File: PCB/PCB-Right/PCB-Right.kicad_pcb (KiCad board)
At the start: 2 copper layers, 109.8 x 71.7 mm, 53 parts, among them J1 USB_C_Receptacle_USB2.0_16P, J2 Conn_ARM_JTAG_SWD_10, Q1 2N7002, SW1 SW_RST, SW2 SW_SPDT, U1 nRF52840_holyiot_18010, U2 XC6206PxxxMR, U3 SRV05-4, U4 BQ24075RGT

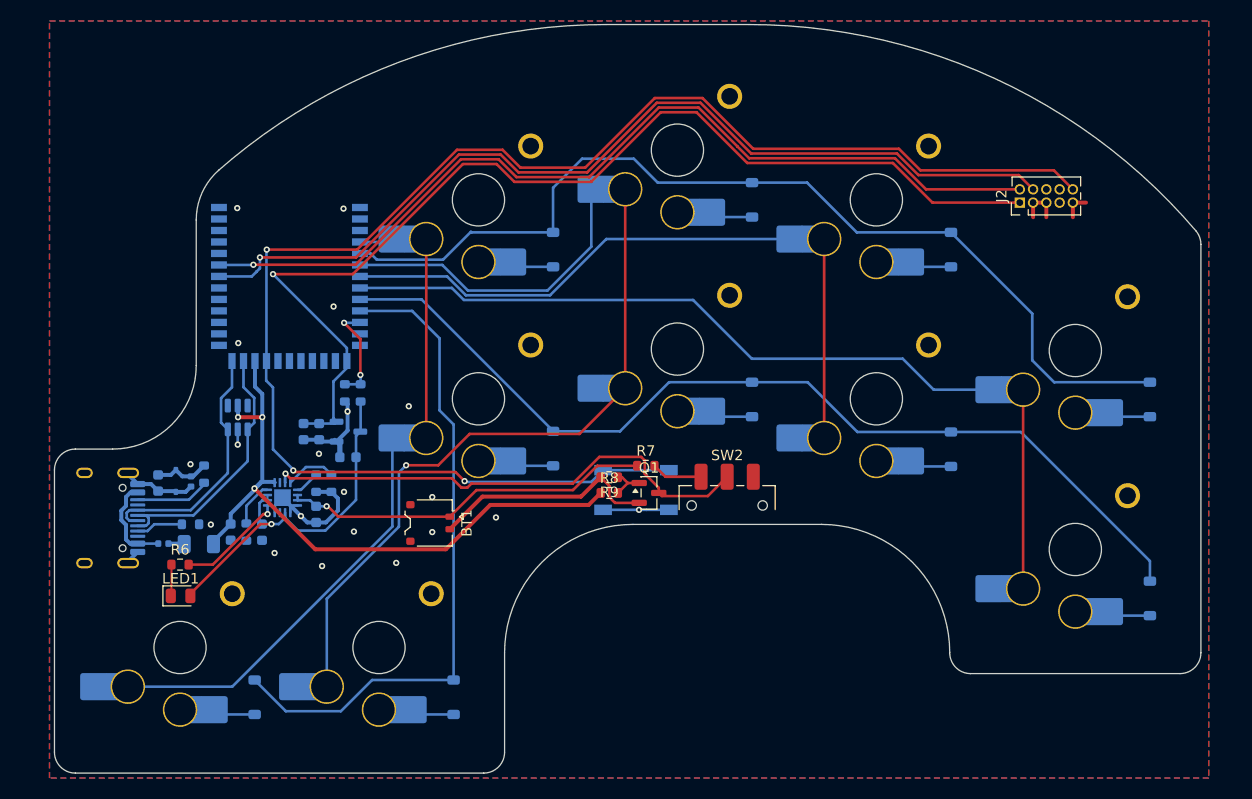
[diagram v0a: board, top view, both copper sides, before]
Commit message: PCB Right
Switched to raytac module
gasket mount
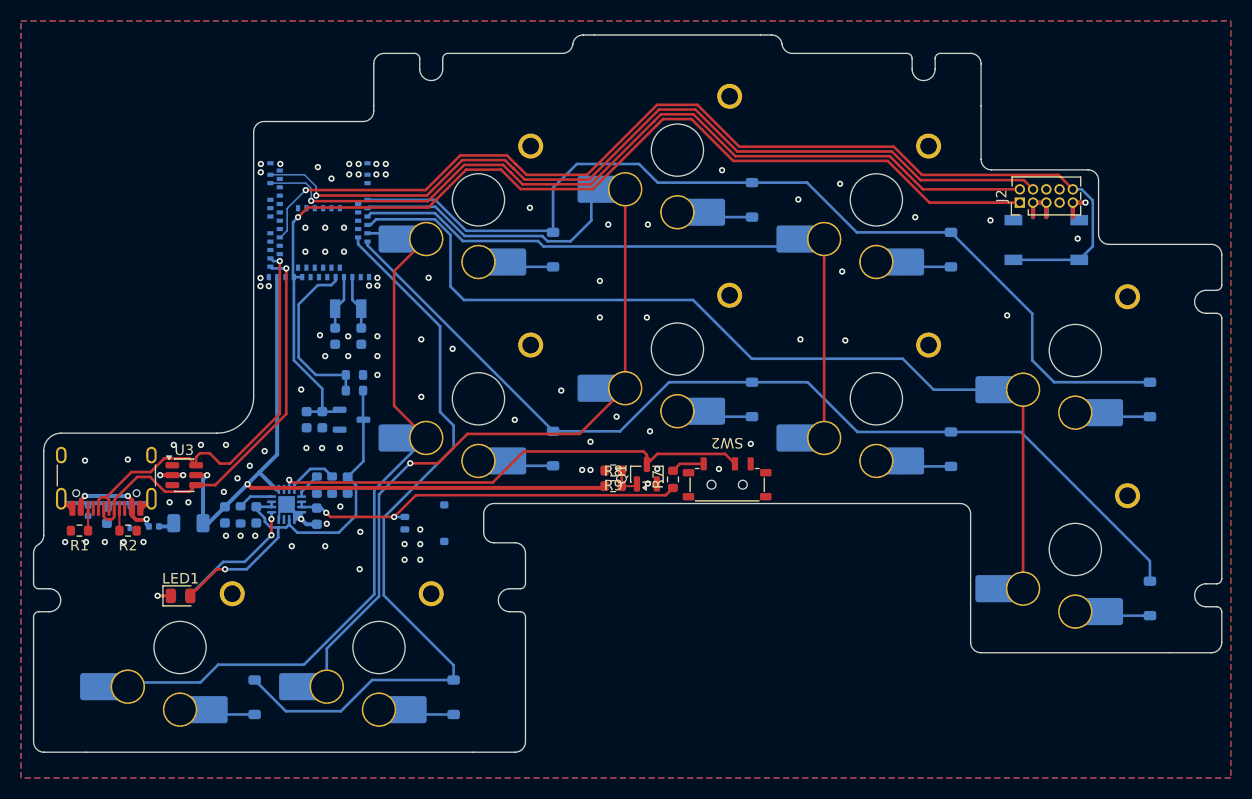
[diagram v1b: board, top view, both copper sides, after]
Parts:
- removed U1: nRF52840_holyiot_18010, marbastlib-various:nRF52840_holyiot_18010_HS_simple
- added C8: 12p, Capacitor_SMD:C_0603_1608Metric, B.Cu at (144.3, 97.2)
- added C9: 12p, Capacitor_SMD:C_0603_1608Metric, B.Cu at (141.8, 97.2)
- added U5: MDBT50Q-1MV2, RF_Module:Raytac_MDBT50Q, B.Cu at (140.3, 84.4)
- added Y1: 32.768KHz, Crystal:Crystal_SMD_3215-2Pin_3.2x1.5mm, B.Cu at (143.1, 94.6)
- BT1, R6: moved to B.Cu
- J1: footprint Connector_USB:USB_C_Receptacle_HRO_TYPE-C-31-M-12 -> marbastlib-various:USB_C_Receptacle_HRO_TYPE-C-31-M-12; moved to F.Cu
- R1, R2, U3: moved to F.Cu
- SW2: footprint Button_Switch_SMD:SW_SPDT_CK_JS102011SAQN -> marbastlib-various:SW_MSK12C02-HB
- moved SW1 46.0 mm to (209.9, 88.0), turned to 0 degrees
- moved R1 13.1 mm to (117.4, 115.8), turned to 180 degrees
- moved L2 10.2 mm to (118.2, 113.9), turned to -90 degrees
- moved U3 7.54 mm to (127.4, 110.5), turned to 0 degrees
- moved R2 6.01 mm to (122.0, 115.8)
- moved C4 5.79 mm to (120.0, 114.3), turned to 90 degrees
- moved D11 5.60 mm to (122.2, 114.5), turned to -90 degrees
- moved J1 5.08 mm to (119.9, 109.6), turned to 180 degrees
- moved R6 2.99 mm to (127.0, 122.1)
- moved R7 2.91 mm to (174.2, 110.9), turned to 90 degrees
- moved C1 2.67 mm to (143.1, 111.5), turned to -90 degrees
- moved F1 2.24 mm to (127.8, 115.1)
- moved SW2 1.99 mm to (179.4, 111.4), turned to 180 degrees
- moved R11 1.95 mm to (143.7, 100.9), turned to 0 degrees
- moved L1 1.87 mm to (124.5, 115.4)
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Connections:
- U3 pad 1: USB-D- -> unconnected-(U3-IO1-Pad1)
- U3 pad 3: USB-D+ -> unconnected-(U3-IO2-Pad3)
- U3 pad 4: unconnected-(U3-IO3-Pad4) -> USB-D-
- U3 pad 6: unconnected-(U3-IO4-Pad6) -> USB-D+
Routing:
- net RST: track 147.4 -> 102.2 mm, vias 3 -> 1
- net GND: track 66.0 -> 27.8 mm, vias 20 -> 101
- net USB-D+: track 24.3 -> 40.2 mm, vias 0 -> 1
- net USB-D-: track 25.8 -> 40.2 mm, vias 0 -> 1
- net row2: track 63.5 -> 73.2 mm
- net SWDCLK: track 90.3 -> 82.5 mm
- net VSENSE: track 9.58 -> 16.4 mm, vias 2 -> 0
- net SWDIO: track 87.6 -> 81.1 mm
- net +5V: track 63.3 -> 69.7 mm, vias 3 -> 2
- net col0: track 62.4 -> 68.2 mm
- net XL2: track 0.00 -> 5.23 mm
- net XL1: track 0.00 -> 5.23 mm
- net col3: track 83.3 -> 88.5 mm
- net Net-(J1-CC2): track 7.13 -> 2.14 mm
- net +VSW: track 35.5 -> 39.6 mm
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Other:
- board size 109.8 x 71.7 mm -> 113.8 x 68.7 mm

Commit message: replace voltage regulator with DCCH inductor
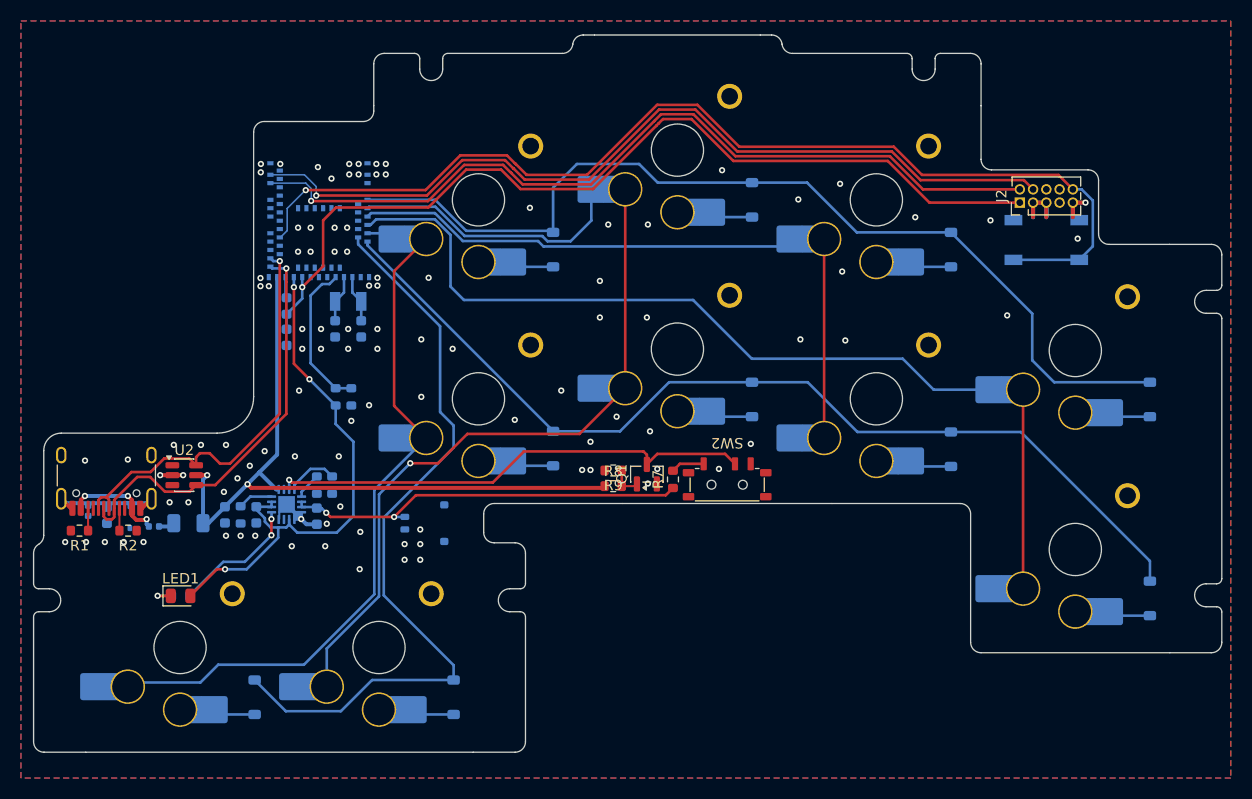
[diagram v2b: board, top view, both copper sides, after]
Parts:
- removed the C2 at (139.1, 105.2)
- removed the C3 at (140.6, 105.2)
- removed the U2 at (143.4, 105.2)
- added L3: 10uH, Inductor_SMD:L_0603_1608Metric, B.Cu at (137.2, 94.3)
- C1: value 1u -> 4u7
- moved C1 15.3 mm to (137.2, 97.3)
- moved R11 2.12 mm to (143.4, 103.0), turned to -90 degrees
- moved R10 1.90 mm to (141.9, 103.0), turned to 90 degrees
- moved C2 0.70 mm to (144.3, 96.5)
- moved C3 0.70 mm to (141.8, 96.5)
- moved Y1 0.70 mm to (143.1, 93.9)
- renumbered C8 to C2, C9 to C3, U3 to U2, U4 to U3
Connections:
- C1 pad 1: +VSW -> VDD
- J2 pad 1: +3.3V -> VDD
- U5 pad 28: +3.3V -> VDD
- U5 pad 30: +3.3V -> +VSW
- U5 pad 31: unconnected-(U5-DCCH-Pad31) -> DCCH
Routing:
- net +3.3V: track 102.0 -> 0.00 mm, vias 1 -> 0
- net VDD: track 0.00 -> 88.6 mm, vias 0 -> 1
- net +VSW: track 39.6 -> 51.6 mm, vias 1 -> 3
- net DCCH: track 0.00 -> 2.02 mm
- net VSENSE: track 16.4 -> 14.5 mm
- net XL2: track 5.23 -> 4.53 mm
- net XL1: track 5.23 -> 4.53 mm
- net GND: vias 101 -> 105

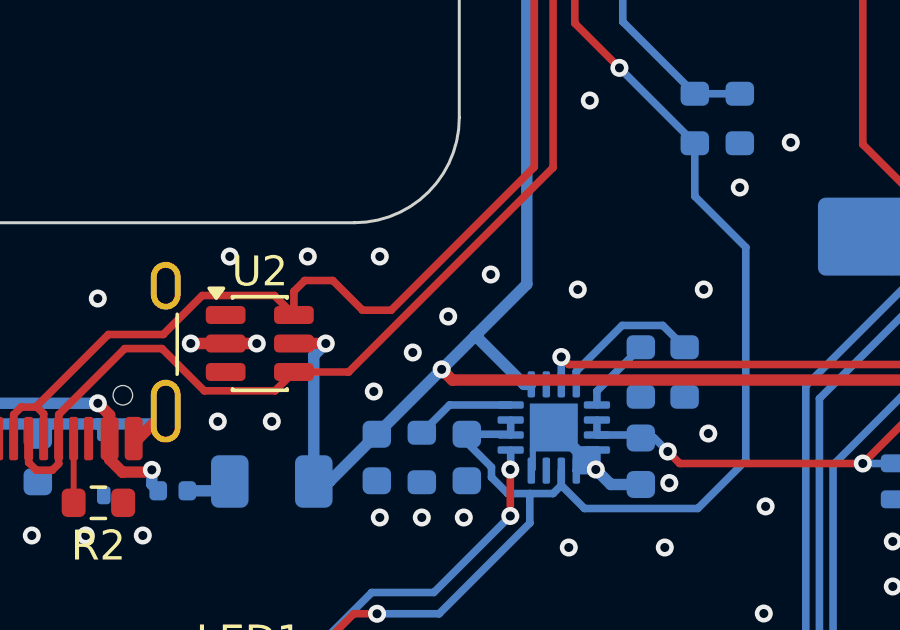
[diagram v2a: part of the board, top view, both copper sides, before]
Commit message: remove backup and lock files
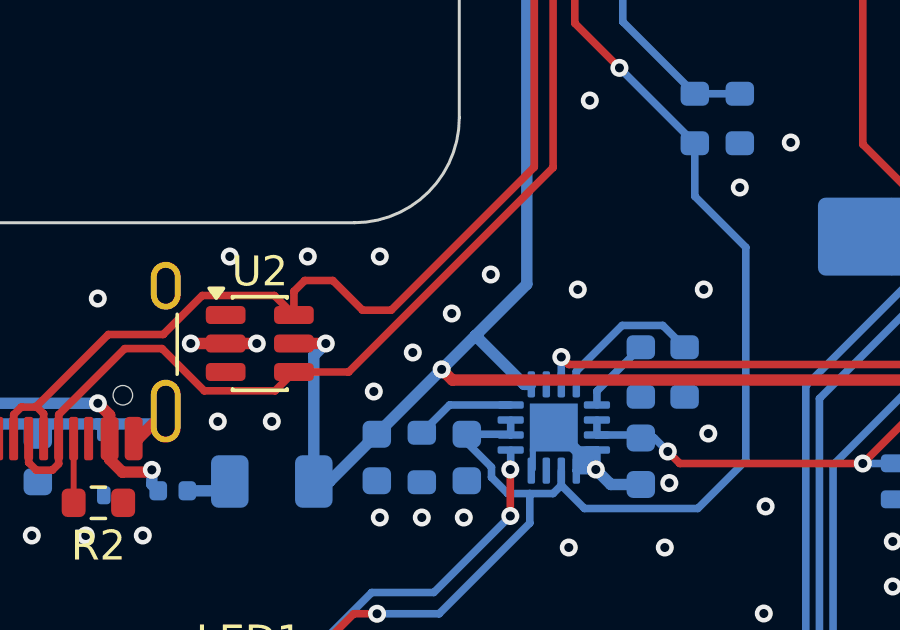
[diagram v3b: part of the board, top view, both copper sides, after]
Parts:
- renumbered U5 to U1
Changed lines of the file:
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@@
 		(descr "Multiprotocol radio SoC module https://www.raytac.com/download/index.php?index_id=43")
 		(tags "wireless 2.4 GHz Bluetooth ble zigbee 802.15.4 thread nordic raytac nrf52840 nrf52833")
-		(property "Reference" "U5"
+		(property "Reference" "U1"
 			(at -6 0 90)
 			(layer "B.SilkS")
@@
 			(size 0.6 0.4)
 			(layers "B.Cu" "B.Mask" "B.Paste")
-			(net "unconnected-(U5-P1.10-Pad3)")
+			(net "unconnected-(U1-P1.10-Pad3)")
 			(pinfunction "P1.10_3")
 			(pintype "bidirectional+no_connect")
@@
 			(size 0.6 0.4)
 			(layers "B.Cu" "B.Mask" "B.Paste")
-			(net "unconnected-(U5-P1.12-Pad5)")
+			(net "unconnected-(U1-P1.12-Pad5)")
 			(pinfunction "P1.12_5")
 			(pintype "bidirectional+no_connect")
@@
 			(size 0.6 0.4)
 			(layers "B.Cu" "B.Mask" "B.Paste")
-			(net "unconnected-(U5-P1.14-Pad7)")
+			(net "unconnected-(U1-P1.14-Pad7)")
 			(pinfunction "P1.14_7")
 			(pintype "bidirectional+no_connect")
@@
 			(size 0.6 0.4)
 			(layers "B.Cu" "B.Mask" "B.Paste")
-			(net "unconnected-(U5-P0.03-Pad9)")
+			(net "unconnected-(U1-P0.03-Pad9)")
 			(pinfunction "P0.03_9")
 			(pintype "bidirectional+no_connect")
@@
 			(size 0.6 0.4)
 			(layers "B.Cu" "B.Mask" "B.Paste")
-			(net "unconnected-(U5-P0.02-Pad11)")
+			(net "unconnected-(U1-P0.02-Pad11)")
 			(pinfunction "P0.02_11")
 			(pintype "bidirectional+no_connect")
@@
 			(size 0.6 0.4)
 			(layers "B.Cu" "B.Mask" "B.Paste")
-			(net "unconnected-(U5-P0.27-Pad16)")
+			(net "unconnected-(U1-P0.27-Pad16)")
 			(pinfunction "P0.27_16")
 			(pintype "bidirectional+no_connect")
@@
 			(size 0.6 0.4)
 			(layers "B.Cu" "B.Mask" "B.Paste")
-			(net "unconnected-(U5-P0.26-Pad19)")
+			(net "unconnected-(U1-P0.26-Pad19)")
 			(pinfunction "P0.26_19")
 			(pintype "bidirectional+no_connect")
@@
 			(size 0.6 0.4)
 			(layers "B.Cu" "B.Mask" "B.Paste")
-			(net "unconnected-(U5-P0.05-Pad21)")
+			(net "unconnected-(U1-P0.05-Pad21)")
 			(pinfunction "P0.05_21")
 			(pintype "bidirectional+no_connect")
@@
 			(size 0.6 0.4)
 			(layers "B.Cu" "B.Mask" "B.Paste")
-			(net "unconnected-(U5-P0.06-Pad22)")
+			(net "unconnected-(U1-P0.06-Pad22)")
 			(pinfunction "P0.06_22")
 			(pintype "bidirectional+no_connect")
@@
 			(size 0.6 0.4)
 			(layers "B.Cu" "B.Mask" "B.Paste")
-			(net "unconnected-(U5-P0.07-Pad23)")
+			(net "unconnected-(U1-P0.07-Pad23)")
 			(pinfunction "P0.07_23")
 			(pintype "bidirectional+no_connect")
@@
 			(size 0.6 0.4)
 			(layers "B.Cu" "B.Mask" "B.Paste")
-			(net "unconnected-(U5-P0.08-Pad24)")
+			(net "unconnected-(U1-P0.08-Pad24)")
 			(pinfunction "P0.08_24")
 			(pintype "bidirectional+no_connect")
@@
 			(size 0.6 0.4)
 			(layers "B.Cu" "B.Mask" "B.Paste")
-			(net "unconnected-(U5-P1.08-Pad25)")
+			(net "unconnected-(U1-P1.08-Pad25)")
 			(pinfunction "P1.08_25")
 			(pintype "bidirectional+no_connect")
@@
 			(size 0.6 0.4)
 			(layers "B.Cu" "B.Mask" "B.Paste")
-			(net "unconnected-(U5-P1.09-Pad26)")
+			(net "unconnected-(U1-P1.09-Pad26)")
 			(pinfunction "P1.09_26")
 			(pintype "bidirectional+no_connect")
@@
 			(size 0.6 0.4)
 			(layers "B.Cu" "B.Mask" "B.Paste")
-			(net "unconnected-(U5-P0.11-Pad27)")
+			(net "unconnected-(U1-P0.11-Pad27)")
 			(pinfunction "P0.11_27")
 			(pintype "bidirectional+no_connect")
@@
 			(size 0.6 0.4)
 			(layers "B.Cu" "B.Mask" "B.Paste")
-			(net "unconnected-(U5-P0.12-Pad29)")
+			(net "unconnected-(U1-P0.12-Pad29)")
 			(pinfunction "P0.12_29")
 			(pintype "bidirectional+no_connect")
@@
 			(size 0.6 0.4)
 			(layers "B.Cu" "B.Mask" "B.Paste")
-			(net "unconnected-(U5-P0.14-Pad36)")
+			(net "unconnected-(U1-P0.14-Pad36)")
 			(pinfunction "P0.14_36")
 			(pintype "bidirectional+no_connect")
@@
 			(size 0.6 0.4)
 			(layers "B.Cu" "B.Mask" "B.Paste")
-			(net "unconnected-(U5-P0.13-Pad37)")
+			(net "unconnected-(U1-P0.13-Pad37)")
 			(pinfunction "P0.13_37")
 			(pintype "bidirectional+no_connect")
@@
 			(size 0.6 0.4)
 			(layers "B.Cu" "B.Mask" "B.Paste")
-			(net "unconnected-(U5-P0.16-Pad38)")
+			(net "unconnected-(U1-P0.16-Pad38)")
 			(pinfunction "P0.16_38")
 			(pintype "bidirectional+no_connect")
@@
 			(size 0.6 0.4)
 			(layers "B.Cu" "B.Mask" "B.Paste")
-			(net "unconnected-(U5-P0.15-Pad39)")
+			(net "unconnected-(U1-P0.15-Pad39)")
 			(pinfunction "P0.15_39")
 			(pintype "bidirectional+no_connect")
@@
 			(size 0.6 0.4)
 			(layers "B.Cu" "B.Mask" "B.Paste")
-			(net "unconnected-(U5-P0.17-Pad41)")
+			(net "unconnected-(U1-P0.17-Pad41)")
 			(pinfunction "P0.17_41")
 			(pintype "bidirectional+no_connect")
@@
 			(size 0.6 0.4)
 			(layers "B.Cu" "B.Mask" "B.Paste")
-			(net "unconnected-(U5-P0.19-Pad42)")
+			(net "unconnected-(U1-P0.19-Pad42)")
 			(pinfunction "P0.19_42")
 			(pintype "bidirectional+no_connect")
@@
 			(size 0.6 0.4)
 			(layers "B.Cu" "B.Mask" "B.Paste")
-			(net "unconnected-(U5-P0.21-Pad43)")
+			(net "unconnected-(U1-P0.21-Pad43)")
 			(pinfunction "P0.21_43")
 			(pintype "bidirectional+no_connect")
@@
 			(size 0.6 0.4)
 			(layers "B.Cu" "B.Mask" "B.Paste")
-			(net "unconnected-(U5-P0.20-Pad44)")
+			(net "unconnected-(U1-P0.20-Pad44)")
 			(pinfunction "P0.20_44")
 			(pintype "bidirectional+no_connect")
@@
 			(size 0.6 0.4)
 			(layers "B.Cu" "B.Mask" "B.Paste")
-			(net "unconnected-(U5-P0.23-Pad45)")
+			(net "unconnected-(U1-P0.23-Pad45)")
 			(pinfunction "P0.23_45")
 			(pintype "bidirectional+no_connect")
@@
 			(size 0.6 0.4)
 			(layers "B.Cu" "B.Mask" "B.Paste")
-			(net "unconnected-(U5-P0.22-Pad46)")
+			(net "unconnected-(U1-P0.22-Pad46)")
 			(pinfunction "P0.22_46")
 			(pintype "bidirectional+no_connect")
@@
 			(size 0.6 0.4)
 			(layers "B.Cu" "B.Mask" "B.Paste")
-			(net "unconnected-(U5-P1.00-Pad47)")
+			(net "unconnected-(U1-P1.00-Pad47)")
 			(pinfunction "P1.00_47")
 			(pintype "bidirectional+no_connect")
@@
 			(size 0.6 0.4)
 			(layers "B.Cu" "B.Mask" "B.Paste")
-			(net "unconnected-(U5-P0.24-Pad48)")
+			(net "unconnected-(U1-P0.24-Pad48)")
 			(pinfunction "P0.24_48")
 			(pintype "bidirectional+no_connect")
@@
 			(size 0.6 0.4)
 			(layers "B.Cu" "B.Mask" "B.Paste")
-			(net "unconnected-(U5-P0.25-Pad49)")
+			(net "unconnected-(U1-P0.25-Pad49)")
 			(pinfunction "P0.25_49")
 			(pintype "bidirectional+no_connect")
@@
 			(size 0.6 0.4)
 			(layers "B.Cu" "B.Mask" "B.Paste")
-			(net "unconnected-(U5-P1.02-Pad50)")
+			(net "unconnected-(U1-P1.02-Pad50)")
 			(pinfunction "P1.02_50")
 			(pintype "bidirectional+no_connect")
@@
 			(size 0.6 0.4)
 			(layers "B.Cu" "B.Mask" "B.Paste")
-			(net "unconnected-(U5-P0.09-Pad52)")
+			(net "unconnected-(U1-P0.09-Pad52)")
 			(pinfunction "P0.09_52")
 			(pintype "bidirectional+no_connect")
@@
 			(size 0.6 0.4)
 			(layers "B.Cu" "B.Mask" "B.Paste")
-			(net "unconnected-(U5-P0.10-Pad54)")
+			(net "unconnected-(U1-P0.10-Pad54)")
 			(pinfunction "P0.10_54")
 			(pintype "bidirectional+no_connect")
@@
 			(size 0.6 0.4)
 			(layers "B.Cu" "B.Mask" "B.Paste")
-			(net "unconnected-(U5-P1.04-Pad56)")
+			(net "unconnected-(U1-P1.04-Pad56)")
 			(pinfunction "P1.04_56")
 			(pintype "bidirectional+no_connect")
@@
 			(size 0.6 0.4)
 			(layers "B.Cu" "B.Mask" "B.Paste")
-			(net "unconnected-(U5-P1.06-Pad57)")
+			(net "unconnected-(U1-P1.06-Pad57)")
 			(pinfunction "P1.06_57")
 			(pintype "bidirectional+no_connect")
@@
 			(size 0.6 0.4)
 			(layers "B.Cu" "B.Mask" "B.Paste")
-			(net "unconnected-(U5-P1.07-Pad58)")
+			(net "unconnected-(U1-P1.07-Pad58)")
 			(pinfunction "P1.07_58")
 			(pintype "bidirectional+no_connect")
@@
 			(size 0.6 0.4)
 			(layers "B.Cu" "B.Mask" "B.Paste")
-			(net "unconnected-(U5-P1.05-Pad59)")
+			(net "unconnected-(U1-P1.05-Pad59)")
 			(pinfunction "P1.05_59")
 			(pintype "bidirectional+no_connect")
@@
 			(size 0.6 0.4)
 			(layers "B.Cu" "B.Mask" "B.Paste")
-			(net "unconnected-(U5-P1.03-Pad60)")
+			(net "unconnected-(U1-P1.03-Pad60)")
 			(pinfunction "P1.03_60")
 			(pintype "bidirectional+no_connect")
@@
 			(size 0.6 0.4)
 			(layers "B.Cu" "B.Mask" "B.Paste")
-			(net "unconnected-(U5-P1.01-Pad61)")
+			(net "unconnected-(U1-P1.01-Pad61)")
 			(pinfunction "P1.01_61")
 			(pintype "bidirectional+no_connect")
@@
 	)
 	(via
-		(at 133.68 109.6)
+		(at 133.8 109.5)
 		(size 0.6)
 		(drill 0.3)
